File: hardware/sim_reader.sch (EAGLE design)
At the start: 15 parts, among them IC1 74AC04D, X1 3.57 MHz

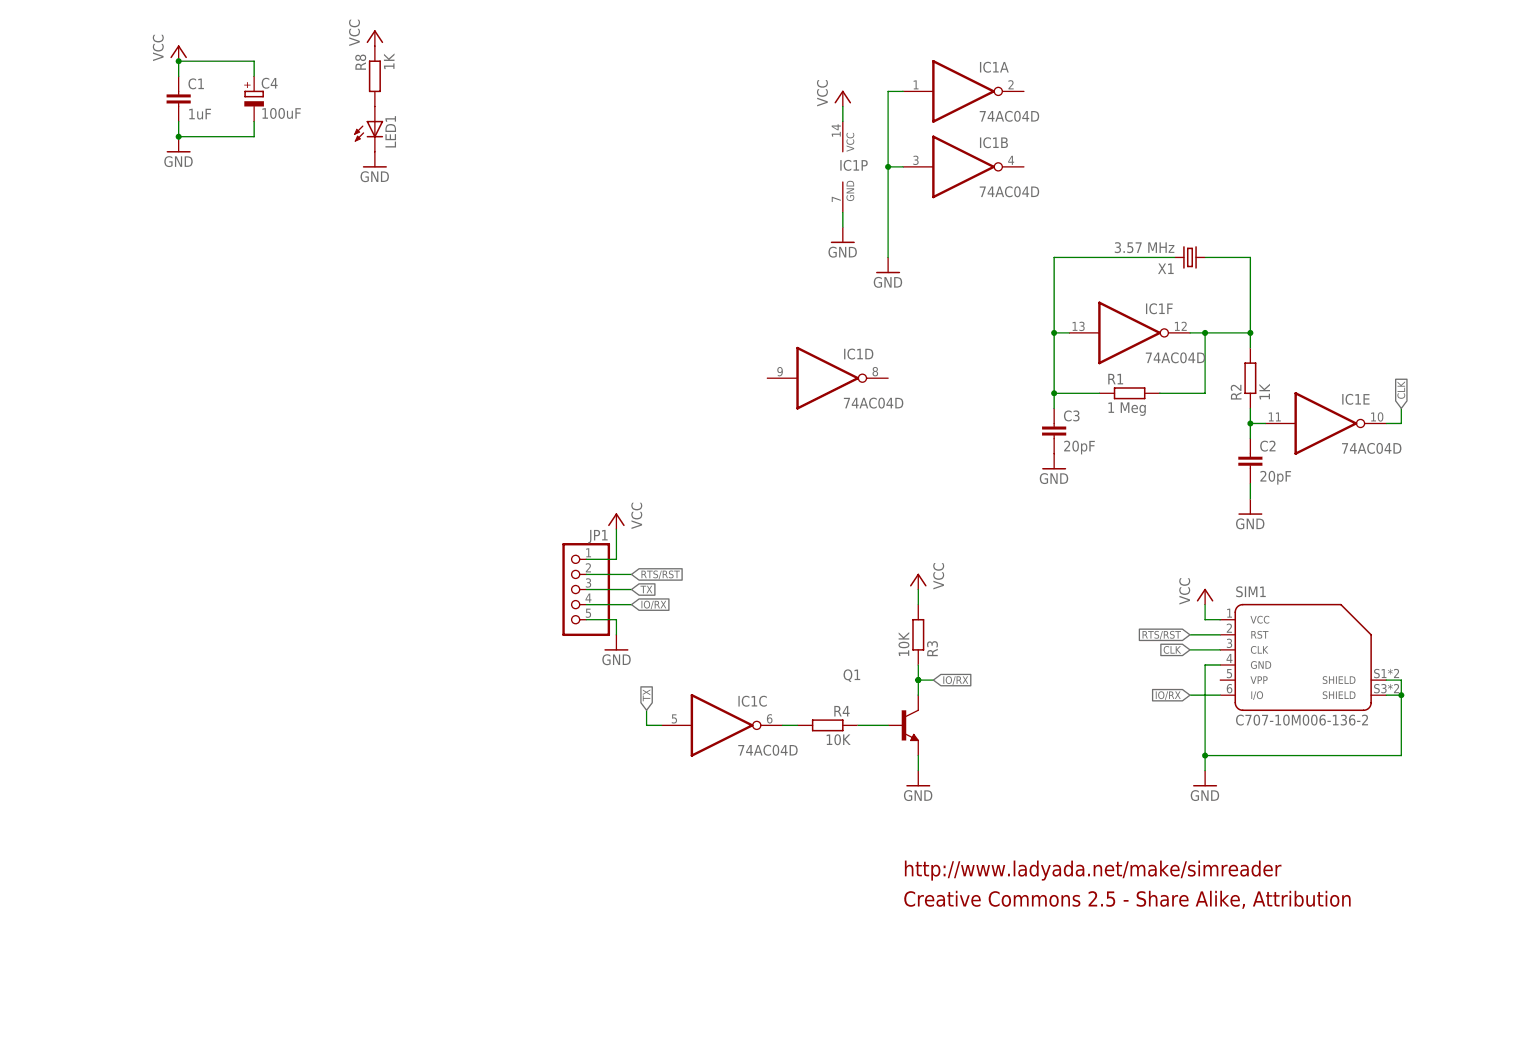
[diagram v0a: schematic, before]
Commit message: redisgned. now compatible to most USB UART converters; very small
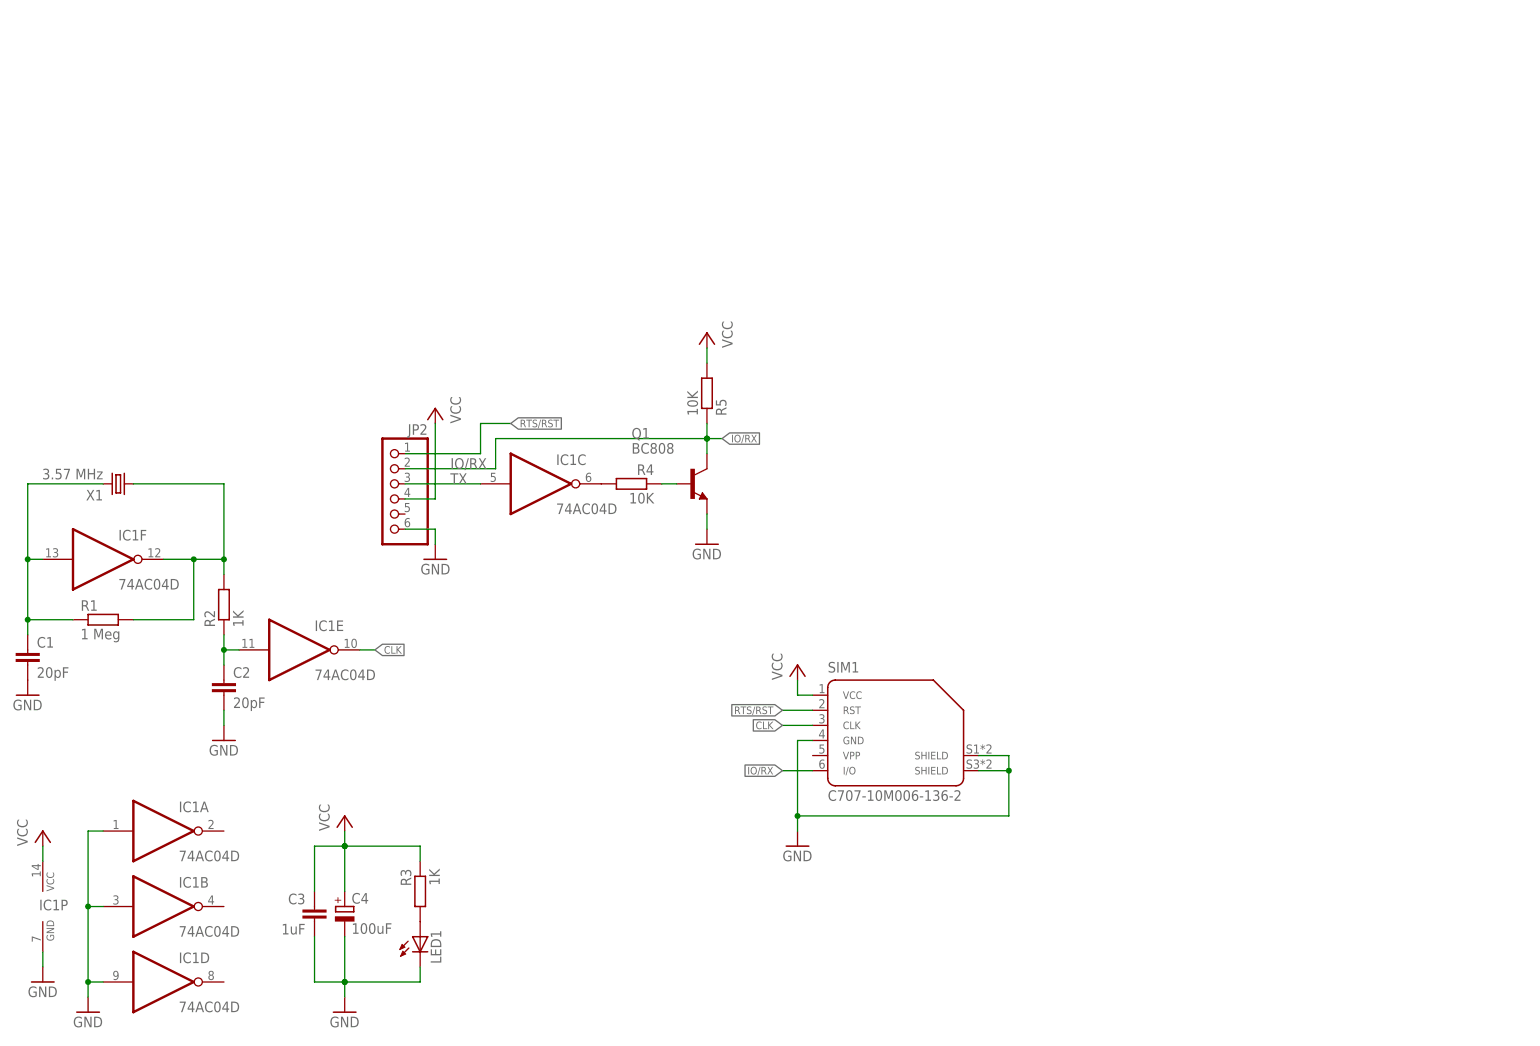
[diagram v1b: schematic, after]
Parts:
- removed JP1: (no value), smd_pinhead:PINHD-1X5
- removed R8: 1K, rcl:R-EU_R0805
- added JP2: (no value), smd_pinhead:PINHD-1X6
- added R5: 10K, rcl:R-EU_R0603
- C1: value 1uF -> 20pF; device rcl:C-EUC0805 -> rcl:C-EUC0603
- C2: device rcl:C-EUC0805 -> rcl:C-EUC0603
- C3: value 20pF -> 1uF; device rcl:C-EUC0805 -> rcl:C-EUC0603
- LED1: device led:LEDCHIPLED_0805 -> led:LEDCHIPLED_0603
- Q1: value (none) -> BC808
- R1, R2, R4: device rcl:R-EU_R0805 -> rcl:R-EU_R0603
- R3: value 10K -> 1K; device rcl:R-EU_R0805 -> rcl:R-EU_R0603
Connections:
- net GND: now also IC1D.I, JP2.6; no longer JP1.5
- net IO/RX: now also JP2.2, R5.1; no longer JP1.4, R3.1
- net N$1: now also C1.1; no longer C3.1
- net N$13: now also R3.2; no longer R8.2
- net RTS/RST: now also JP2.1; no longer JP1.2
- net TX: now also JP2.3; no longer JP1.3
- net VCC: now also C3.1, JP2.4, R3.1, R5.2; no longer C1.1, JP1.1, R3.2, R8.1
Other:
- note removed: "Creative Commons 2.5 - Share Alike, Attribution"
- note removed: "http://www.ladyada.net/make/simreader"
- moved on the sheet: C1, C2, C3, C4, IC1A, IC1B, IC1C, IC1D, IC1E, IC1F, IC1P, LED1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
